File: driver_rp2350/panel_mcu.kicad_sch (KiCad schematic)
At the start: 32 parts, among them SW1 SW_Push, SW2 SW_Push, U1 W25Q16JVUXIQ_TR, U2 RP2350_80QFN, Y1 ABM8-272-T3

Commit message: Worked on modifications for converting rp2350 design to 18x18 array.
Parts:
- C1, C10, C11, C12, C13, C14, C15, C16, C17, C18, C2, C3, C6, C9: footprint Capacitor_SMD:C_0402_1005Metric -> Capacitor_SMD:C_0201_0603Metric
- C19: footprint Capacitor_SMD:C_0805_2012Metric -> Capacitor_SMD:C_0402_1005Metric
- R1, R2, R3, R4, R5, R6, R7: footprint Resistor_SMD:R_0402_1005Metric -> Resistor_SMD:R_0201_0603Metric
- SW1, SW2: footprint Button_Switch_SMD:SW_Push_1P1T_NO_Vertical_Wuerth_434133025816 -> panel_custom:TS-1088-AR02016
- U1: footprint W25Q16JVUXIQ_TR:PSON50P300X200X60-9N -> panel_custom:flashmem_PSON50P300X200X60-9N
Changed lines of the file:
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@@
 			)
 		)
-		(property "Footprint" "Capacitor_SMD:C_0402_1005Metric"
+		(property "Footprint" "Capacitor_SMD:C_0201_0603Metric"
 			(at 60.96 119.0752 0)
 			(effects
@@
 			)
 		)
-		(property "Footprint" "Capacitor_SMD:C_0402_1005Metric"
+		(property "Footprint" "Capacitor_SMD:C_0201_0603Metric"
 			(at 60.96 129.2352 0)
 			(effects
@@
 			)
 		)
-		(property "Footprint" "Capacitor_SMD:C_0402_1005Metric"
+		(property "Footprint" "Capacitor_SMD:C_0201_0603Metric"
 			(at 258.7752 40.64 0)
 			(effects
@@
 			)
 		)
-		(property "Footprint" "Capacitor_SMD:C_0402_1005Metric"
+		(property "Footprint" "Capacitor_SMD:C_0201_0603Metric"
 			(at 270.2052 40.64 0)
 			(effects
@@
 			)
 		)
-		(property "Footprint" "Capacitor_SMD:C_0402_1005Metric"
+		(property "Footprint" "Capacitor_SMD:C_0201_0603Metric"
 			(at 281.6352 40.64 0)
 			(effects
@@
 			)
 		)
-		(property "Footprint" "Capacitor_SMD:C_0402_1005Metric"
+		(property "Footprint" "Capacitor_SMD:C_0201_0603Metric"
 			(at 293.0652 40.64 0)
 			(effects
@@
 			)
 		)
-		(property "Footprint" "Capacitor_SMD:C_0402_1005Metric"
+		(property "Footprint" "Capacitor_SMD:C_0201_0603Metric"
 			(at 304.4952 40.64 0)
 			(effects
@@
 			)
 		)
-		(property "Footprint" "Capacitor_SMD:C_0402_1005Metric"
+		(property "Footprint" "Capacitor_SMD:C_0201_0603Metric"
 			(at 315.9252 40.64 0)
 			(effects
@@
 			)
 		)
-		(property "Footprint" "Capacitor_SMD:C_0805_2012Metric"
+		(property "Footprint" "Capacitor_SMD:C_0402_1005Metric"
 			(at 338.7852 40.64 0)
 			(effects
@@
 			)
 		)
-		(property "Footprint" "Capacitor_SMD:C_0402_1005Metric"
+		(property "Footprint" "Capacitor_SMD:C_0201_0603Metric"
 			(at 173.6852 40.64 0)
 			(effects
@@
 			)
 		)
-		(property "Footprint" "Resistor_SMD:R_0402_1005Metric"
+		(property "Footprint" "Resistor_SMD:R_0201_0603Metric"
 			(at 256.54 64.262 90)
 			(effects
@@
 			)
 		)
-		(property "Footprint" "Capacitor_SMD:C_0402_1005Metric"
+		(property "Footprint" "Capacitor_SMD:C_0201_0603Metric"
 			(at 247.3452 40.64 0)
 			(effects
@@
 			)
 		)
-		(property "Footprint" "Capacitor_SMD:C_0402_1005Metric"
+		(property "Footprint" "Capacitor_SMD:C_0201_0603Metric"
 			(at 327.3552 40.64 0)
 			(effects
@@
 			)
 		)
-		(property "Footprint" "Button_Switch_SMD:SW_Push_1P1T_NO_Vertical_Wuerth_434133025816"
+		(property "Footprint" "panel_custom:TS-1088-AR02016"
 			(at 139.7 130.81 0)
 			(effects
@@
 			)
 		)
-		(property "Footprint" "Resistor_SMD:R_0402_1005Metric"
+		(property "Footprint" "Resistor_SMD:R_0201_0603Metric"
 			(at 152.4 92.202 90)
 			(effects
@@
 			)
 		)
-		(property "Footprint" "Resistor_SMD:R_0402_1005Metric"
+		(property "Footprint" "Resistor_SMD:R_0201_0603Metric"
 			(at 97.79 126.492 90)
 			(effects
@@
 			)
 		)
-		(property "Footprint" "Capacitor_SMD:C_0402_1005Metric"
+		(property "Footprint" "Capacitor_SMD:C_0201_0603Metric"
 			(at 150.8252 40.64 0)
 			(effects
@@
 			)
 		)
-		(property "Footprint" "Capacitor_SMD:C_0402_1005Metric"
+		(property "Footprint" "Capacitor_SMD:C_0201_0603Metric"
 			(at 96.2152 81.28 0)
 			(effects
@@
 			)
 		)
-		(property "Footprint" "Capacitor_SMD:C_0402_1005Metric"
+		(property "Footprint" "Capacitor_SMD:C_0201_0603Metric"
 			(at 235.9152 40.64 0)
 			(effects
@@
 			)
 		)
-		(property "Footprint" "W25Q16JVUXIQ_TR:PSON50P300X200X60-9N"
+		(property "Footprint" "panel_custom:flashmem_PSON50P300X200X60-9N"
 			(at 74.93 77.47 0)
 			(effects
@@
 			)
 		)
-		(property "Footprint" "Resistor_SMD:R_0402_1005Metric"
+		(property "Footprint" "Resistor_SMD:R_0201_0603Metric"
 			(at 127 134.112 90)
 			(effects
@@
 			)
 		)
-		(property "Footprint" "Resistor_SMD:R_0402_1005Metric"
+		(property "Footprint" "Resistor_SMD:R_0201_0603Metric"
 			(at 148.59 62.738 90)
 			(effects
@@
 			)
 		)
-		(property "Footprint" "Button_Switch_SMD:SW_Push_1P1T_NO_Vertical_Wuerth_434133025816"
+		(property "Footprint" "panel_custom:TS-1088-AR02016"
 			(at 130.81 101.6 0)
 			(effects
@@
 			)
 		)
-		(property "Footprint" "Resistor_SMD:R_0402_1005Metric"
+		(property "Footprint" "Resistor_SMD:R_0201_0603Metric"
 			(at 256.54 73.152 90)
 			(effects
@@
 			)
 		)
-		(property "Footprint" "Resistor_SMD:R_0402_1005Metric"
+		(property "Footprint" "Resistor_SMD:R_0201_0603Metric"
 			(at 56.388 58.42 90)
 			(effects

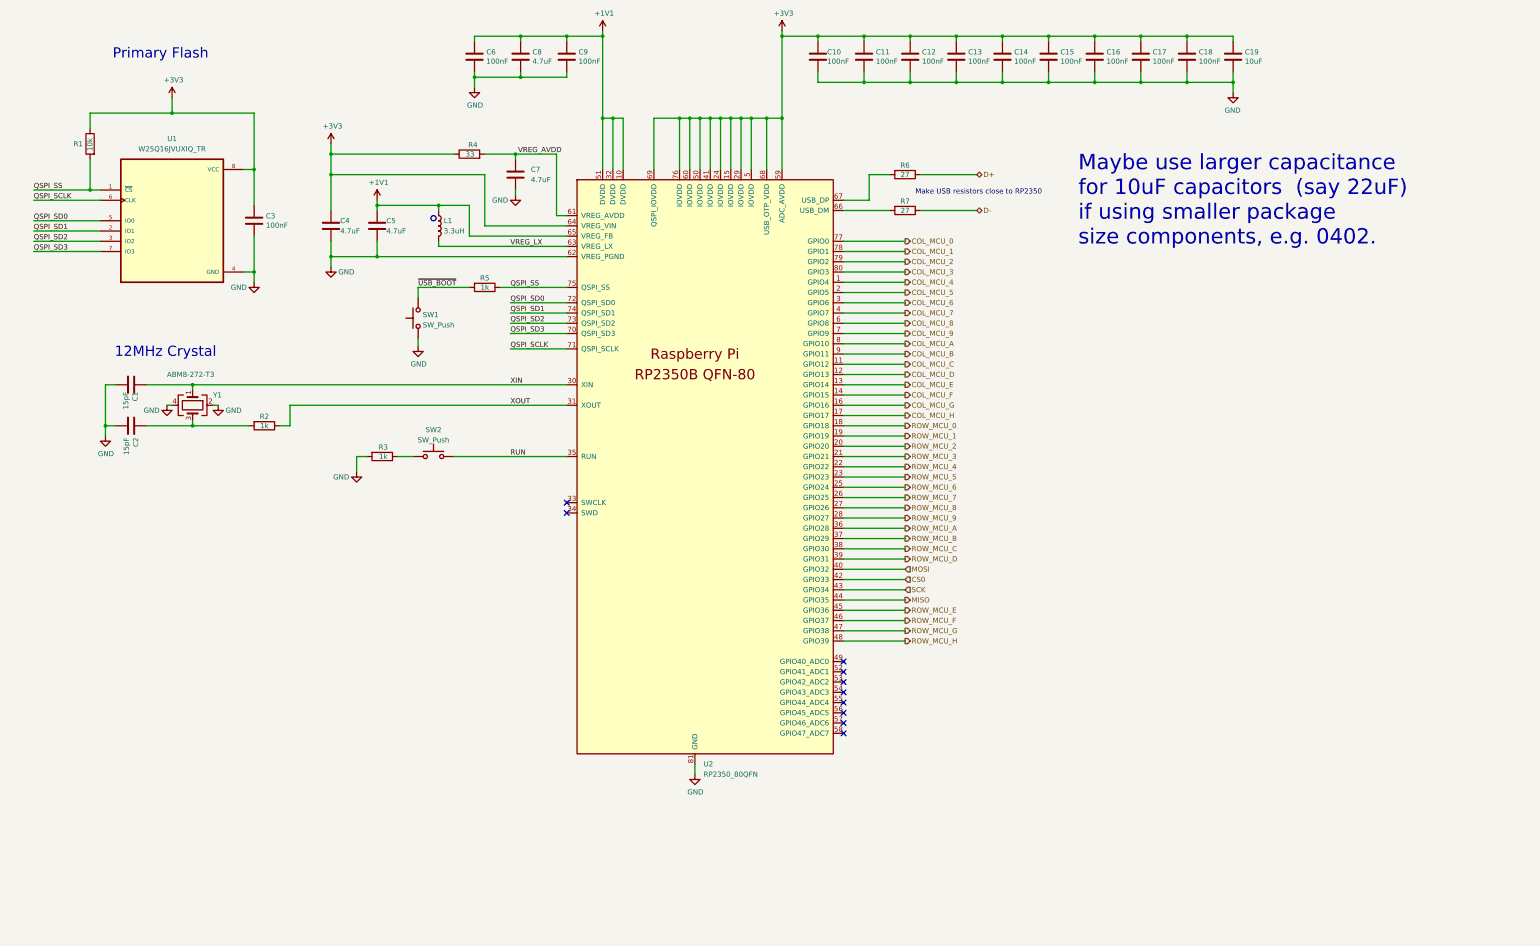
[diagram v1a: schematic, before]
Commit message: Modified for rp2354.
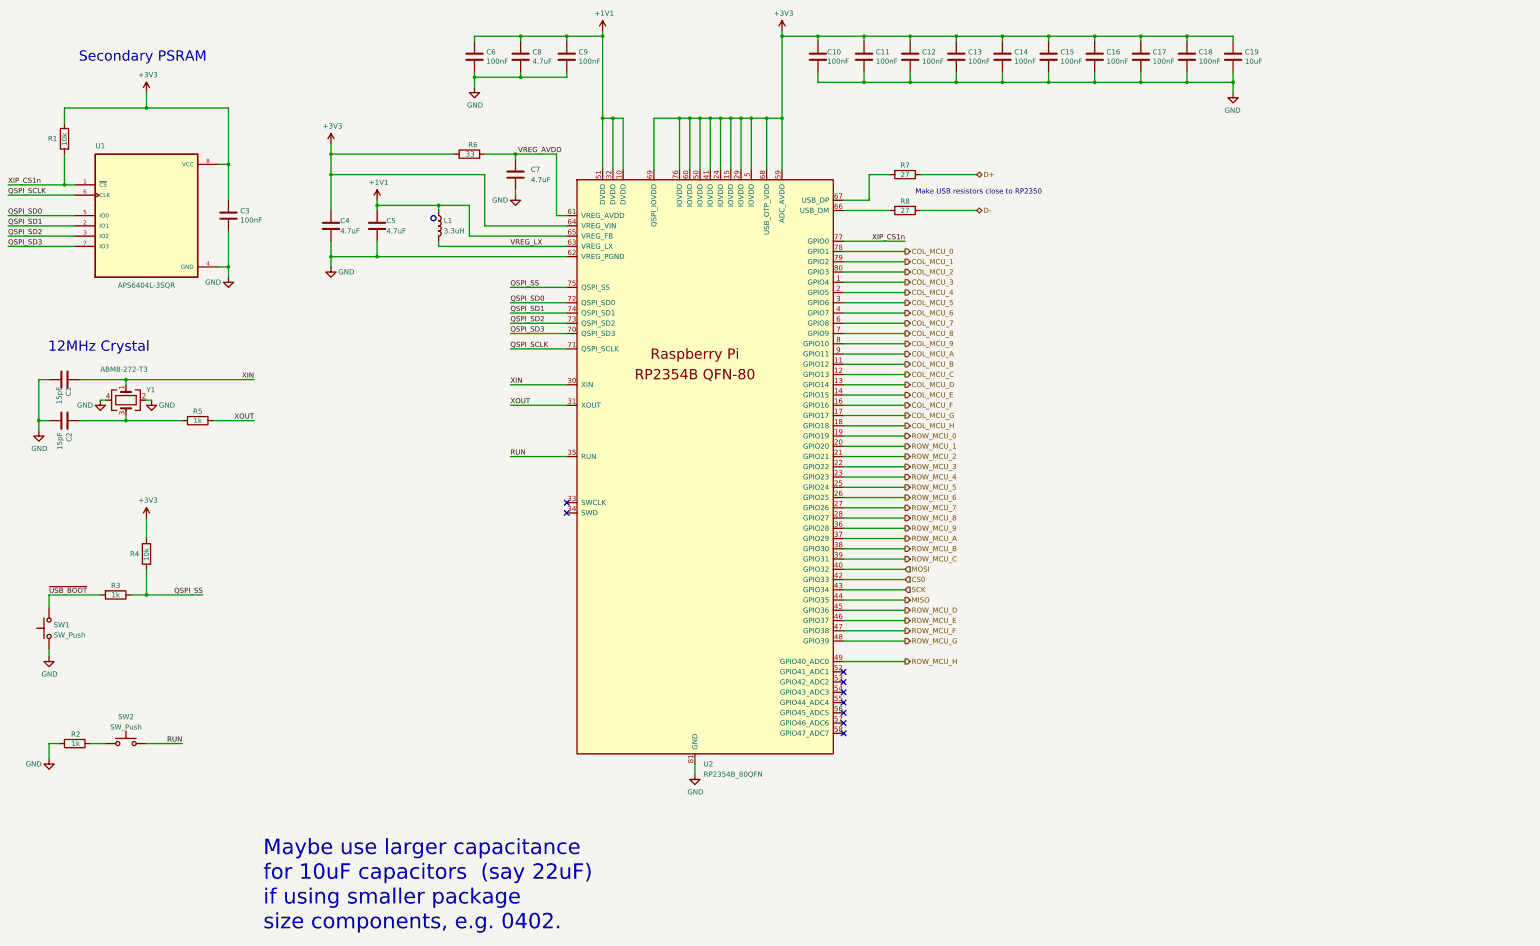
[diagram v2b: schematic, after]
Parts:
- removed U1: W25Q16JVUXIQ_TR, panel_custom:flashmem_PSON50P300X200X60-9N, symbol panel_custom:W25Q16JVUXIQ_TR
- removed U2: RP2350_80QFN, RP2350_80QFN_minimal:RP2350-QFN-80-1EP_10x10_P0.4mm_EP3.4x3.4mm_ThermalVias, symbol MCU_RaspberryPi_RP2350:RP2350_80QFN
- added R4: 10k, Resistor_SMD:R_0201_0603Metric, symbol Device:R
- added U1: APS6404L-3SQR, panel_custom:flashmem_PSON50P300X200X60-9N, symbol panel_custom:APS6404L-3SQR
- added U2: RP2354B_80QFN, RP2350_80QFN_minimal:RP2350-QFN-80-1EP_10x10_P0.4mm_EP3.4x3.4mm_ThermalVias, symbol panel_custom:RP2354B_80QFN
- renumbered R3 to R2, R5 to R3, R2 to R5, R4 to R6, R6 to R7, R7 to R8
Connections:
- net +1V1: now also U2.10 (DVDD), U2.32 (DVDD), U2.51 (DVDD), U2.65 (VREG_FB)
- net +3V3: now also R4.1, U1.8 (VCC), U2.15 (IOVDD), U2.24 (IOVDD), U2.29 (IOVDD), U2.41 (IOVDD), U2.5 (IOVDD), U2.50 (IOVDD), U2.59 (ADC_AVDD), U2.60 (IOVDD), U2.64 (VREG_VIN), U2.68 (USB_OTP_VDD), U2.69 (QSPI_IOVDD), U2.76 (IOVDD)
- net COL_MCU_0: now also U2.78 (GPIO1)
- net COL_MCU_1: now also U2.79 (GPIO2)
- net COL_MCU_2: now also U2.80 (GPIO3)
- net COL_MCU_3: now also U2.1 (GPIO4)
- net COL_MCU_4: now also U2.2 (GPIO5)
- net COL_MCU_5: now also U2.3 (GPIO6)
- net COL_MCU_6: now also U2.4 (GPIO7)
- net COL_MCU_7: now also U2.6 (GPIO8)
- net COL_MCU_8: now also U2.7 (GPIO9)
- net COL_MCU_9: now also U2.8 (GPIO10)
- net COL_MCU_A: now also U2.9 (GPIO11)
- net COL_MCU_B: now also U2.11 (GPIO12)
- net COL_MCU_C: now also U2.12 (GPIO13)
- net COL_MCU_D: now also U2.13 (GPIO14)
- net COL_MCU_E: now also U2.14 (GPIO15)
- net COL_MCU_F: now also U2.16 (GPIO16)
- net COL_MCU_G: now also U2.17 (GPIO17)
- net COL_MCU_H: now also U2.18 (GPIO18)
- net CS0: now also U2.42 (GPIO33)
- net GND: now also U1.4 (GND), U2.62 (VREG_PGND), U2.81 (GND)
- net MISO: now also U2.44 (GPIO35)
- net MOSI: now also U2.40 (GPIO32)
- net QSPI_SCLK: now also U1.6 (CLK), U2.71 (QSPI_SCLK)
- net QSPI_SD0: now also U1.5 (IO0), U2.72 (QSPI_SD0)
- net QSPI_SD1: now also U1.2 (IO1), U2.74 (QSPI_SD1)
- net QSPI_SD2: now also U1.3 (IO2), U2.73 (QSPI_SD2)
- net QSPI_SD3: now also U1.7 (IO3), U2.70 (QSPI_SD3)
- net QSPI_SS: now also R4.2, U2.75 (QSPI_SS); no longer R1.2
- net ROW_MCU_0: now also U2.19 (GPIO19)
- net ROW_MCU_1: now also U2.20 (GPIO20)
- net ROW_MCU_2: now also U2.21 (GPIO21)
- net ROW_MCU_3: now also U2.22 (GPIO22)
- net ROW_MCU_4: now also U2.23 (GPIO23)
- net ROW_MCU_5: now also U2.25 (GPIO24)
- net ROW_MCU_6: now also U2.26 (GPIO25)
- net ROW_MCU_7: now also U2.27 (GPIO26)
- net ROW_MCU_8: now also U2.28 (GPIO27)
- net ROW_MCU_9: now also U2.36 (GPIO28)
- net ROW_MCU_A: now also U2.37 (GPIO29)
- net ROW_MCU_B: now also U2.38 (GPIO30)
- net ROW_MCU_C: now also U2.39 (GPIO31)
- net ROW_MCU_D: now also U2.45 (GPIO36)
- net ROW_MCU_E: now also U2.46 (GPIO37)
- net ROW_MCU_F: now also U2.47 (GPIO38)
- net ROW_MCU_G: now also U2.48 (GPIO39)
- net ROW_MCU_H: now also U2.49 (GPIO40_ADC0)
- net RUN: now also U2.35 (RUN)
- net SCK: now also U2.43 (GPIO34)
- net VREG_AVDD: now also U2.61 (VREG_AVDD)
- net VREG_LX: now also U2.63 (VREG_LX)
- net XIN: now also U2.30 (XIN)
- net XOUT: now also U2.31 (XOUT)
- net at R7.2: now also U2.67 (USB_DP)
- net at R8.2: now also U2.66 (USB_DM)
- new net XIP_CS1n: R1.2, U1.1 (~{CS}), U2.77 (GPIO0)
- no-connect marks 10 -> 9
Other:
- note added: "Secondary PSRAM"
- note removed: "Primary Flash"
- moved on the sheet: C1, C2, C3, R1, R2, R3, R5, SW1, SW2, Y1
